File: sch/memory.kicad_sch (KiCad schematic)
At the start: 6 parts

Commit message: Memory Module
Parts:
- removed UMUX1: 74LS151, Package_DIP:DIP-18_W7.62mm_SMDSocket_SmallPads, symbol 74xx:74LS151
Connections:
- net CPU_R/~{W}: now also ROM1.24 (OE)
- net D0: now also RAM0.2 (A16), RAM1.2 (A16), RAM2.2 (A16), RAM3.2 (A16)
- net D1: now also RAM0.1 (A17), RAM1.1 (A17), RAM2.1 (A17), RAM3.1 (A17)
- net D2: now also RAM0.30 (A18), RAM1.30 (A18), RAM2.30 (A18), RAM3.30 (A18)
- net ~{RAM2_EN}: now reaches RAM2.22 (~{CE})
- net ~{RAM2_EN}: now also RAM2.24 (~{OE})
- net CPU_W/~{R}: now reaches RAM2.29 (~{WE})
- net CPU_W/~{R}: now also RAM0.29 (~{WE}), RAM1.29 (~{WE}), RAM3.29 (~{WE})
- net ~{RAM1_EN}: now reaches RAM1.22 (~{CE})
- net ~{RAM1_EN}: now also RAM1.24 (~{OE})
- net ~{RAM0_EN}: now reaches RAM0.22 (~{CE})
- net ~{RAM0_EN}: now also RAM0.24 (~{OE})
- net ~{RAM3_EN}: now reaches RAM3.22 (~{CE})
- net ~{RAM3_EN}: now also RAM3.24 (~{OE})
- net CROM_EN: now reaches ROM1.2 (A16)
- net ROM_EN: now reaches ROM1.22 (CE)
- removed net READ: RAM0.24 (~{OE}), RAM1.24 (~{OE}), RAM2.24 (~{OE}), RAM3.24 (~{OE}), ROM1.24 (OE), ROM1.31 (PGM)
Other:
- added sheet Address Decoder (decoder.kicad_sch)
- note added: "Expansion Space"
- note added: "High if CPU is reading from DATA BUS"
- note added: "High if DATA BUS is used as ADDR HIGH bits"
- note added: "RAM"
- note added: "ROM & Chars"
- moved on the sheet: RAM0, RAM1, RAM2, RAM3, ROM1

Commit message: Bus control
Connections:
- net D0: no longer RAM0.2 (A16), RAM1.2 (A16), RAM2.2 (A16), RAM3.2 (A16)
- net D1: no longer RAM0.1 (A17), RAM1.1 (A17), RAM2.1 (A17), RAM3.1 (A17)
- net D2: no longer RAM0.30 (A18), RAM1.30 (A18), RAM2.30 (A18), RAM3.30 (A18)
- new net A16: RAM0.2 (A16), RAM1.2 (A16), RAM2.2 (A16), RAM3.2 (A16)
- new net A17: RAM0.1 (A17), RAM1.1 (A17), RAM2.1 (A17), RAM3.1 (A17)
- new net A18: RAM0.30 (A18), RAM1.30 (A18), RAM2.30 (A18), RAM3.30 (A18)
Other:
- sheet Address Decoder ports: added A[0..23]; removed CPU_A/~{D}, MEM{D[0..7]}
- note removed: "High if DATA BUS is used as ADDR HIGH bits"

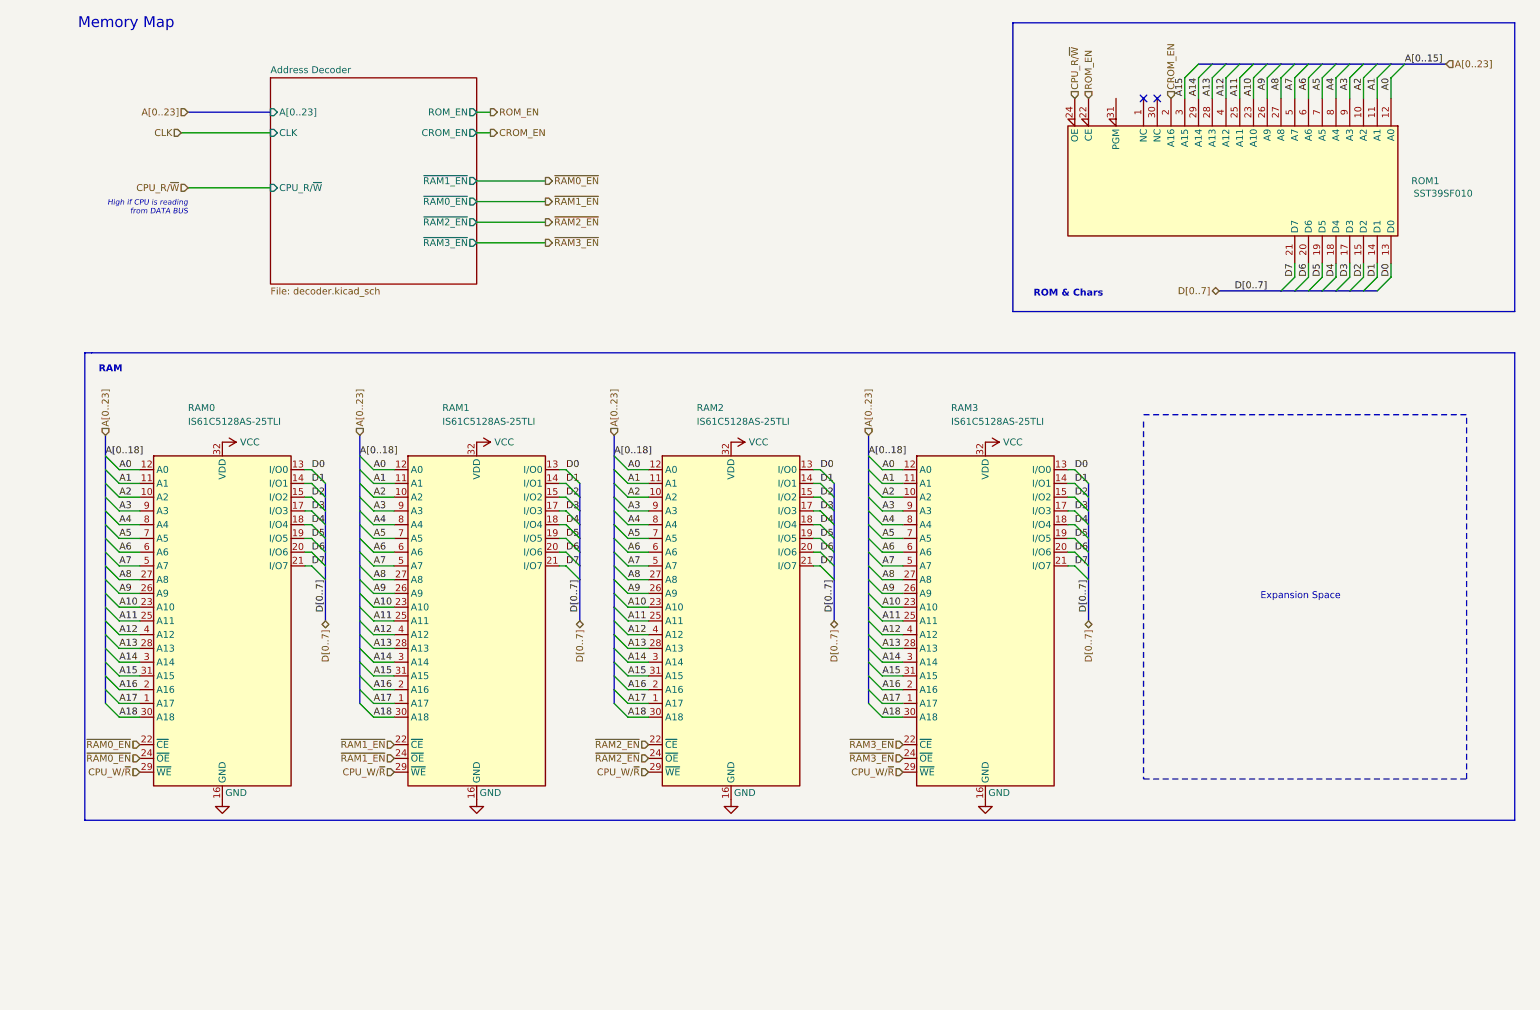
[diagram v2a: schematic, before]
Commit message: New address decoder
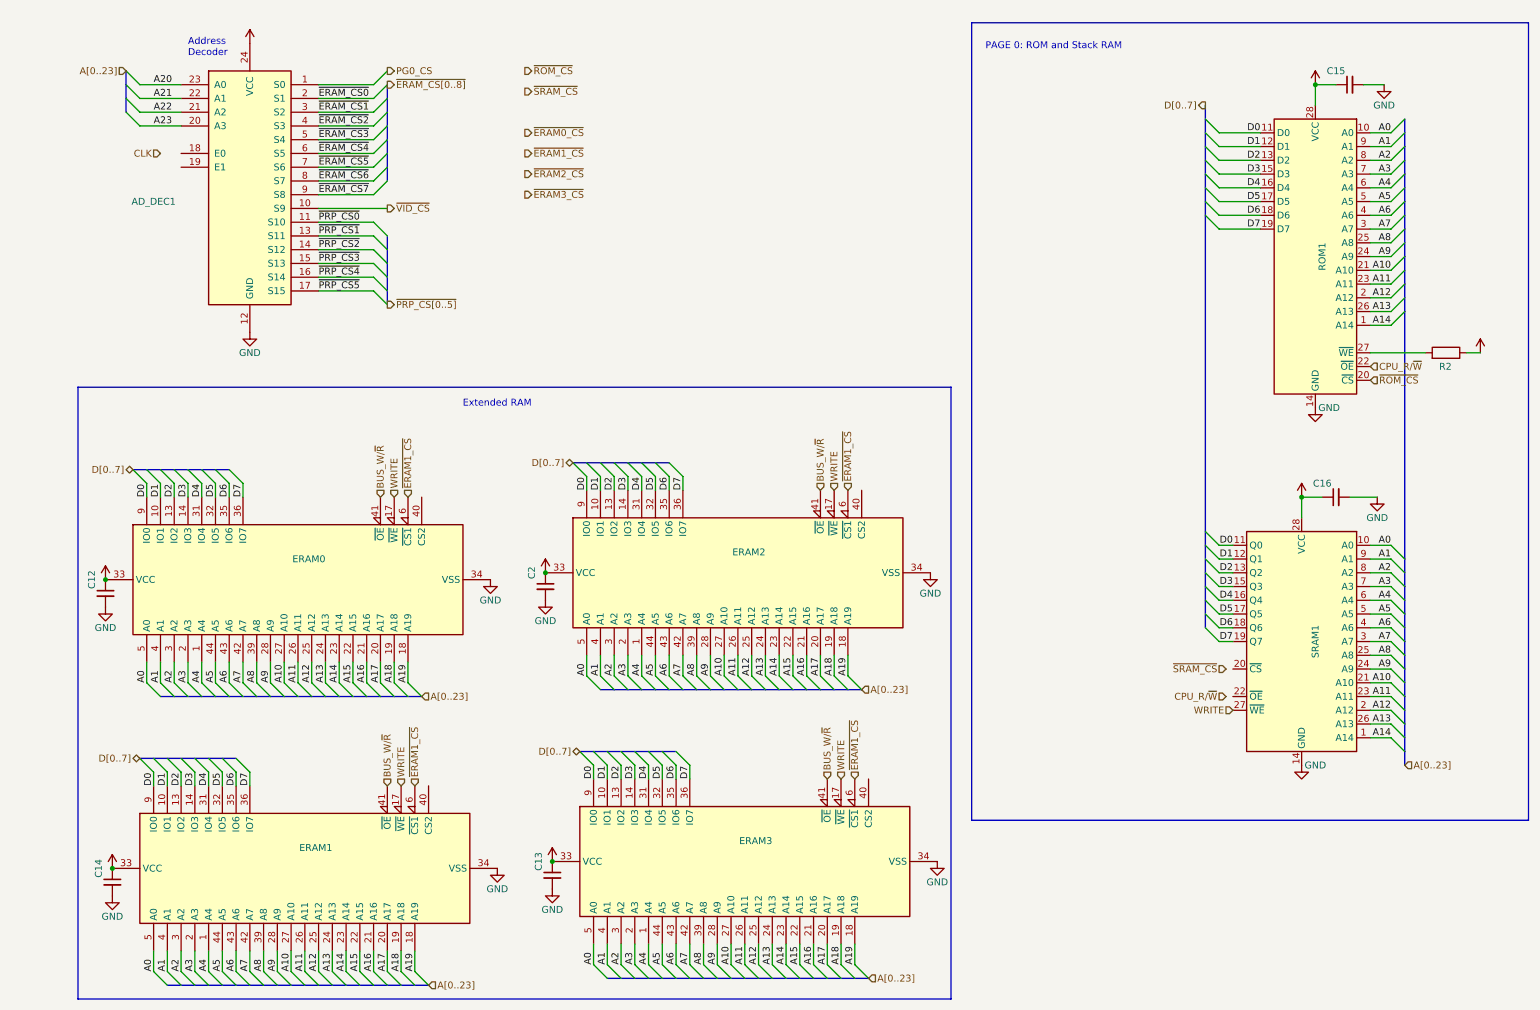
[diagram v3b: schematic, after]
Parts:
- removed RAM0, RAM1, RAM2, RAM3: IS61C5128AS-25TLI, Package_SO:TSOP-II-32_21.0x10.2mm_P1.27mm, symbol Memory_RAM:IS61C5128AS-25TLI
- removed ROM1: SST39SF010, Package_DIP:DIP-32_W15.24mm_LongPads, symbol Memory_Flash:SST39SF010
- added AD_DEC1: (no value), symbol 74xx:74LS154
- added C12, C13, C14, C15, C16, C2: (no value), symbol Device:C_Small
- added ERAM0, ERAM1, ERAM2, ERAM3: (no value), Package_SO:TSOP-II-44_10.16x18.41mm_P0.8mm, symbol Custom:IS62WV10248
- added R2: (no value), symbol Device:R
- added ROM1: (no value), symbol Memory_EEPROM:28C256
- added SRAM1: (no value), symbol Memory_RAM:KM62256CLP
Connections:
- net A0: now also ERAM0.5 (A0), ERAM1.5 (A0), ERAM2.5 (A0), ERAM3.5 (A0), ROM1.10 (A0), SRAM1.10 (A0)
- net A1: now also ERAM0.4 (A1), ERAM1.4 (A1), ERAM2.4 (A1), ERAM3.4 (A1), ROM1.9 (A1), SRAM1.9 (A1)
- net A10: now also ERAM0.27 (A10), ERAM1.27 (A10), ERAM2.27 (A10), ERAM3.27 (A10), ROM1.21 (A10), SRAM1.21 (A10)
- net A11: now also ERAM0.26 (A11), ERAM1.26 (A11), ERAM2.26 (A11), ERAM3.26 (A11), ROM1.23 (A11), SRAM1.23 (A11)
- net A12: now also ERAM0.25 (A12), ERAM1.25 (A12), ERAM2.25 (A12), ERAM3.25 (A12), ROM1.2 (A12), SRAM1.2 (A12)
- net A13: now also ERAM0.24 (A13), ERAM1.24 (A13), ERAM2.24 (A13), ERAM3.24 (A13), ROM1.26 (A13), SRAM1.26 (A13)
- net A14: now also ERAM0.23 (A14), ERAM1.23 (A14), ERAM2.23 (A14), ERAM3.23 (A14), ROM1.1 (A14), SRAM1.1 (A14)
- net A15: now also ERAM0.22 (A15), ERAM1.22 (A15), ERAM2.22 (A15), ERAM3.22 (A15)
- net A16: now also ERAM0.21 (A16), ERAM1.21 (A16), ERAM2.21 (A16), ERAM3.21 (A16)
- net A17: now also ERAM0.20 (A17), ERAM1.20 (A17), ERAM2.20 (A17), ERAM3.20 (A17)
- net A18: now also ERAM0.19 (A18), ERAM1.19 (A18), ERAM2.19 (A18), ERAM3.19 (A18)
- net A2: now also ERAM0.3 (A2), ERAM1.3 (A2), ERAM2.3 (A2), ERAM3.3 (A2), ROM1.8 (A2), SRAM1.8 (A2)
- net A3: now also ERAM0.2 (A3), ERAM1.2 (A3), ERAM2.2 (A3), ERAM3.2 (A3), ROM1.7 (A3), SRAM1.7 (A3)
- net A4: now also ERAM0.1 (A4), ERAM1.1 (A4), ERAM2.1 (A4), ERAM3.1 (A4), ROM1.6 (A4), SRAM1.6 (A4)
- net A5: now also ERAM0.44 (A5), ERAM1.44 (A5), ERAM2.44 (A5), ERAM3.44 (A5), ROM1.5 (A5), SRAM1.5 (A5)
- net A6: now also ERAM0.43 (A6), ERAM1.43 (A6), ERAM2.43 (A6), ERAM3.43 (A6), ROM1.4 (A6), SRAM1.4 (A6)
- net A7: now also ERAM0.42 (A7), ERAM1.42 (A7), ERAM2.42 (A7), ERAM3.42 (A7), ROM1.3 (A7), SRAM1.3 (A7)
- net A8: now also ERAM0.39 (A8), ERAM1.39 (A8), ERAM2.39 (A8), ERAM3.39 (A8), ROM1.25 (A8), SRAM1.25 (A8)
- net A9: now also ERAM0.28 (A9), ERAM1.28 (A9), ERAM2.28 (A9), ERAM3.28 (A9), ROM1.24 (A9), SRAM1.24 (A9)
- net CPU_R/~{W}: now also ROM1.22 (~{OE})
- net D0: now also ERAM0.9 (IO0), ERAM1.9 (IO0), ERAM2.9 (IO0), ERAM3.9 (IO0), ROM1.11 (D0), SRAM1.11 (Q0)
- net D1: now also ERAM0.10 (IO1), ERAM1.10 (IO1), ERAM2.10 (IO1), ERAM3.10 (IO1), ROM1.12 (D1), SRAM1.12 (Q1)
- net D2: now also ERAM0.13 (IO2), ERAM1.13 (IO2), ERAM2.13 (IO2), ERAM3.13 (IO2), ROM1.13 (D2), SRAM1.13 (Q2)
- net D3: now also ERAM0.14 (IO3), ERAM1.14 (IO3), ERAM2.14 (IO3), ERAM3.14 (IO3), ROM1.15 (D3), SRAM1.15 (Q3)
- net D4: now also ERAM0.31 (IO4), ERAM1.31 (IO4), ERAM2.31 (IO4), ERAM3.31 (IO4), ROM1.16 (D4), SRAM1.16 (Q4)
- net D5: now also ERAM0.32 (IO5), ERAM1.32 (IO5), ERAM2.32 (IO5), ERAM3.32 (IO5), ROM1.17 (D5), SRAM1.17 (Q5)
- net D6: now also ERAM0.35 (IO6), ERAM1.35 (IO6), ERAM2.35 (IO6), ERAM3.35 (IO6), ROM1.18 (D6), SRAM1.18 (Q6)
- net D7: now also ERAM0.36 (IO7), ERAM1.36 (IO7), ERAM2.36 (IO7), ERAM3.36 (IO7), ROM1.19 (D7), SRAM1.19 (Q7)
- net GND: now also AD_DEC1.12 (GND), C12.2, C13.2, C14.2, C15.2, C16.2, C2.2, ERAM0.34 (VSS), ERAM1.34 (VSS), ERAM2.34 (VSS), ERAM3.34 (VSS), ROM1.14 (GND), SRAM1.14 (GND)
- new net: R2.2, ROM1.27 (~{WE})
- new net +5V: AD_DEC1.24 (VCC), C12.1, C13.1, C14.1, C15.1, C16.1, C2.1, ERAM0.33 (VCC), ERAM1.33 (VCC), ERAM2.33 (VCC), ERAM3.33 (VCC), R2.1, ROM1.28 (VCC), SRAM1.28 (VCC)
- new net A19: ERAM0.18 (A19), ERAM1.18 (A19), ERAM2.18 (A19), ERAM3.18 (A19)
- new net A20: AD_DEC1.23 (A0)
- new net A21: AD_DEC1.22 (A1)
- new net A22: AD_DEC1.21 (A2)
- new net A23: AD_DEC1.20 (A3)
- new net BUS_W/~{R}: ERAM0.41 (~{OE}), ERAM1.41 (~{OE}), ERAM2.41 (~{OE}), ERAM3.41 (~{OE})
- new net PG0_CS: AD_DEC1.1 (S0)
- new net WRITE: ERAM0.17 (~{WE}), ERAM1.17 (~{WE}), ERAM2.17 (~{WE}), ERAM3.17 (~{WE}), SRAM1.27 (~{WE})
- new net ~{ERAM1_CS}: ERAM0.6 (~{CS1}), ERAM1.6 (~{CS1}), ERAM2.6 (~{CS1}), ERAM3.6 (~{CS1})
- new net ~{ERAM_CS0}: AD_DEC1.2 (S1)
- new net ~{ERAM_CS1}: AD_DEC1.3 (S2)
- new net ~{ERAM_CS2}: AD_DEC1.4 (S3)
- new net ~{ERAM_CS3}: AD_DEC1.5 (S4)
- new net ~{ERAM_CS4}: AD_DEC1.6 (S5)
- new net ~{ERAM_CS5}: AD_DEC1.7 (S6)
- new net ~{ERAM_CS6}: AD_DEC1.8 (S7)
- new net ~{ERAM_CS7}: AD_DEC1.9 (S8)
- new net ~{PRP_CS0}: AD_DEC1.11 (S10)
- new net ~{PRP_CS1}: AD_DEC1.13 (S11)
- new net ~{PRP_CS2}: AD_DEC1.14 (S12)
- new net ~{PRP_CS3}: AD_DEC1.15 (S13)
- new net ~{PRP_CS4}: AD_DEC1.16 (S14)
- new net ~{PRP_CS5}: AD_DEC1.17 (S15)
- new net ~{ROM_CS}: ROM1.20 (~{CS})
- new net ~{VID_CS}: AD_DEC1.10 (S9)
- no-connect marks 2 -> 0
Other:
- removed sheet Address Decoder
- note added: "Address Decoder"
- note added: "Extended RAM"
- note added: "PAGE 0: ROM and Stack RAM"
- note removed: "Expansion Space"
- note removed: "High if CPU is reading from DATA BUS"
- note removed: "Memory Map"
- note removed: "RAM"
- note removed: "ROM & Chars"

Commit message: Board layout, addr bus
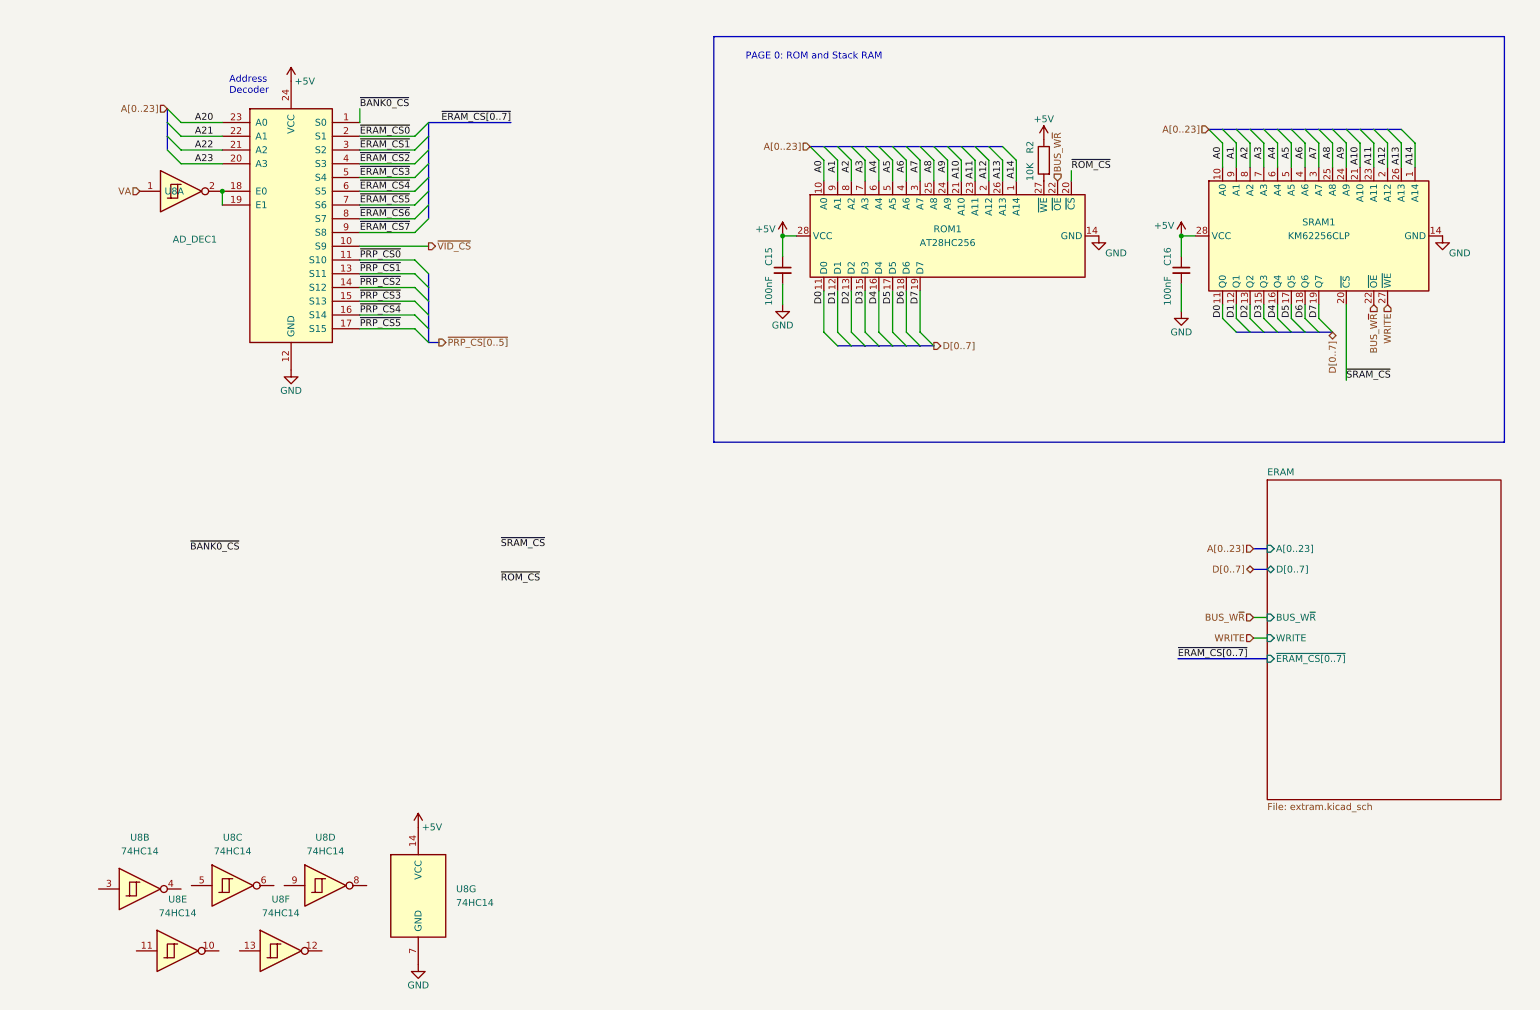
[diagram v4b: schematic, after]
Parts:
- removed C12, C13, C14, C2: (no value), symbol Device:C_Small
- removed ERAM0, ERAM1, ERAM2, ERAM3: (no value), Package_SO:TSOP-II-44_10.16x18.41mm_P0.8mm, symbol Custom:IS62WV10248
- added U8: 74HC14, symbol 74xx:74HC14
- C15, C16: value (none) -> 100nF; footprint (none) -> Capacitor_SMD:C_1206_3216Metric_Pad1.33x1.80mm_HandSolder
- R2: value (none) -> 10K; footprint (none) -> Resistor_SMD:R_1206_3216Metric_Pad1.30x1.75mm_HandSolder
- ROM1: value (none) -> AT28HC256; footprint (none) -> Package_DIP:DIP-28_W15.24mm_LongPads
- SRAM1: value (none) -> KM62256CLP; footprint (none) -> Package_DIP:DIP-28_W15.24mm
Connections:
- net CPU_R/~{W} is gone; now on net BUS_W~{R}: ROM1.22 (~{OE})
- net +5V: now also U8.14 (VCC)
- net GND: now also U8.7 (GND)
- net ~{SRAM_CS}: now also SRAM1.20 (~{CS})
- net at AD_DEC1.18 (E0): now also AD_DEC1.19 (E1), U8.2
- net BUS_W~{R}: now reaches SRAM1.22 (~{OE})
- net PG0_CS renamed ~{BANK0_CS}
- new net VA: U8.1
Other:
- added sheet ERAM (extram.kicad_sch)
- note removed: "Extended RAM"
- moved on the sheet: AD_DEC1, C15, C16, R2, ROM1, SRAM1

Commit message: More routing, USB iface
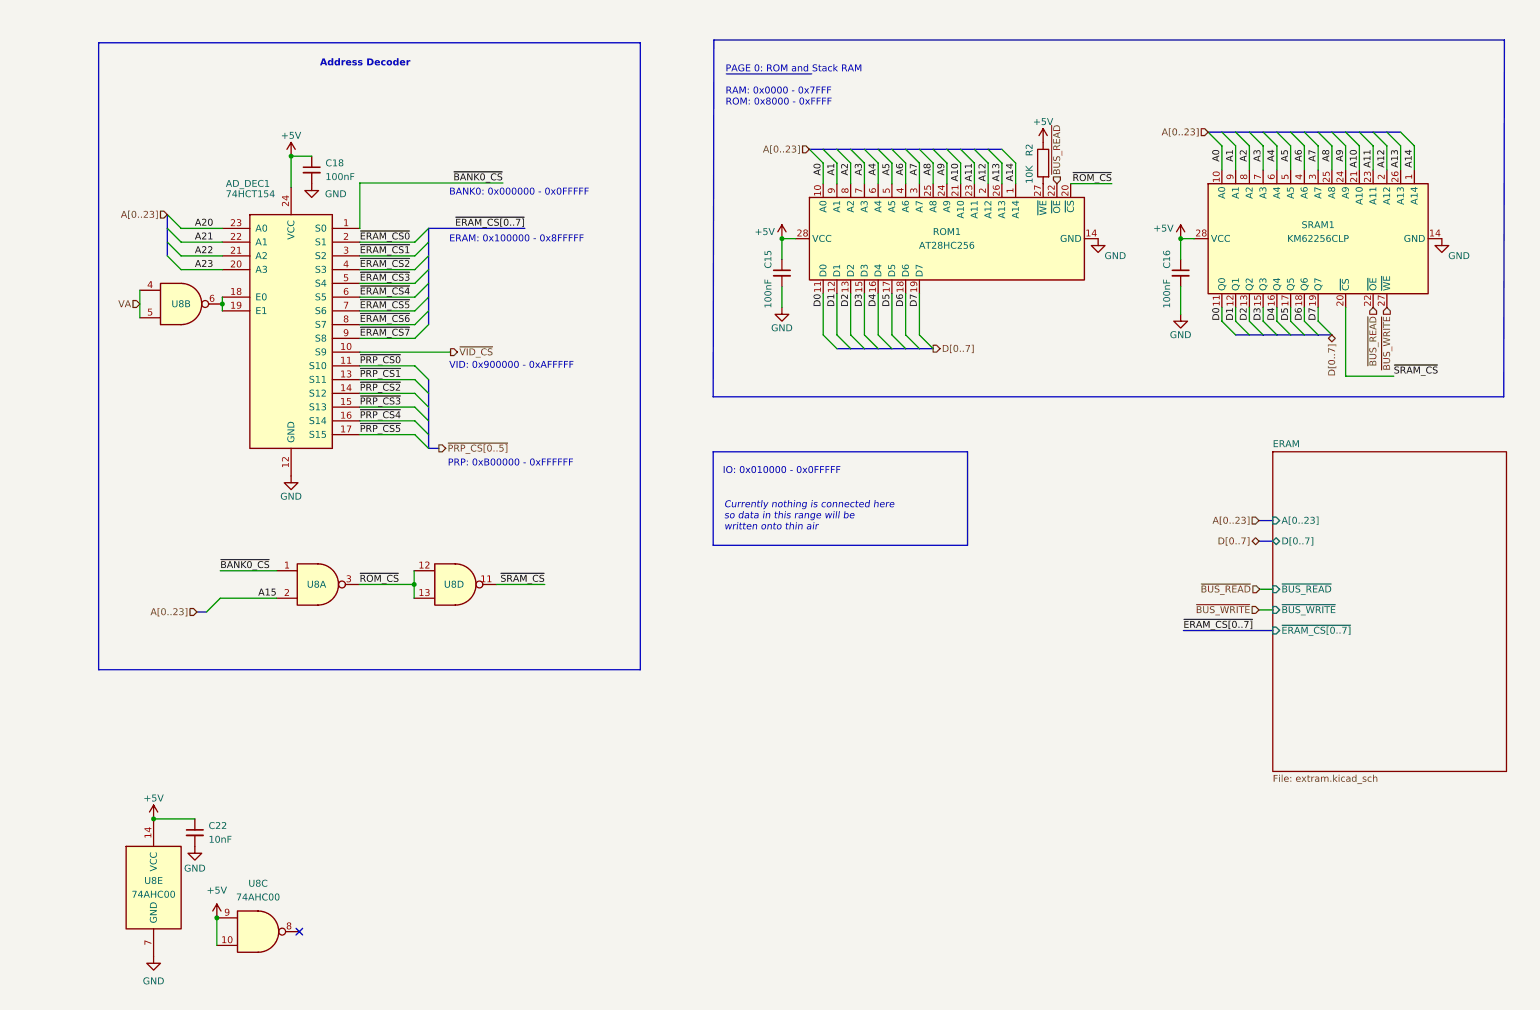
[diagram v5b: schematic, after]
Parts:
- removed U8: 74HC14, symbol 74xx:74HC14
- added C18: 100nF, Capacitor_SMD:C_1206_3216Metric_Pad1.33x1.80mm_HandSolder, symbol Device:C_Small
- added C22: 10nF, Capacitor_SMD:C_0603_1608Metric, symbol Device:C_Small
- added U8: 74AHC00, Package_SO:TSSOP-14_4.4x5mm_P0.65mm, symbol 74xx:74HC00
- AD_DEC1: value (none) -> 74HCT154; footprint (none) -> Package_SO:SO-24_5.3x15mm_P1.27mm
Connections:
- net +5V: now also C18.1, C22.1, U8.10, U8.14 (VCC), U8.9
- net GND: now also C18.2, C22.2, U8.7 (GND)
- net VA: now also U8.4, U8.5
- net ~{BANK0_CS}: now also U8.1
- net ~{ROM_CS}: now also U8.12, U8.13, U8.3
- net ~{SRAM_CS}: now also U8.11
- net at AD_DEC1.18 (E0), AD_DEC1.19 (E1): now also U8.6
- net BUS_W~{R} renamed ~{BUS_READ}
- net WRITE renamed ~{BUS_WRITE}
- new net A15: U8.2
- no-connect marks 0 -> 1
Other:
- sheet ERAM ports: added ~{BUS_READ}, ~{BUS_WRITE}; removed BUS_W~{R}, WRITE
- note added: "BANK0: 0x000000 - 0x0FFFFF"
- note added: "Currently nothing is connected here so data in this range will be written onto thin air"
- note added: "ERAM: 0x100000 - 0x8FFFFF"
- note added: "IO: 0x010000 - 0x0FFFFF"
- note added: "PAGE 0: ROM and Stack RAM ~{ } RAM: 0x0000 - 0x7FFF ROM: 0x8000 - 0xFFFF"
- note added: "PRP: 0xB00000 - 0xFFFFFF"
- note added: "VID: 0x900000 - 0xAFFFFF"
- note removed: "PAGE 0: ROM and Stack RAM"
- moved on the sheet: AD_DEC1, C15, C16, R2, ROM1, SRAM1

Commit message: Pivot to 6502
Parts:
- ROM1: value AT28HC256 -> AT28C256
- SRAM1: value KM62256CLP -> AS6C62256-55PCN
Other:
- note added: "ZERO: 0x000000 - 0x0FFFFF"
- note removed: "BANK0: 0x000000 - 0x0FFFFF"
